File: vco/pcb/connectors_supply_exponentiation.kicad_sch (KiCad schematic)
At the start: 49 parts

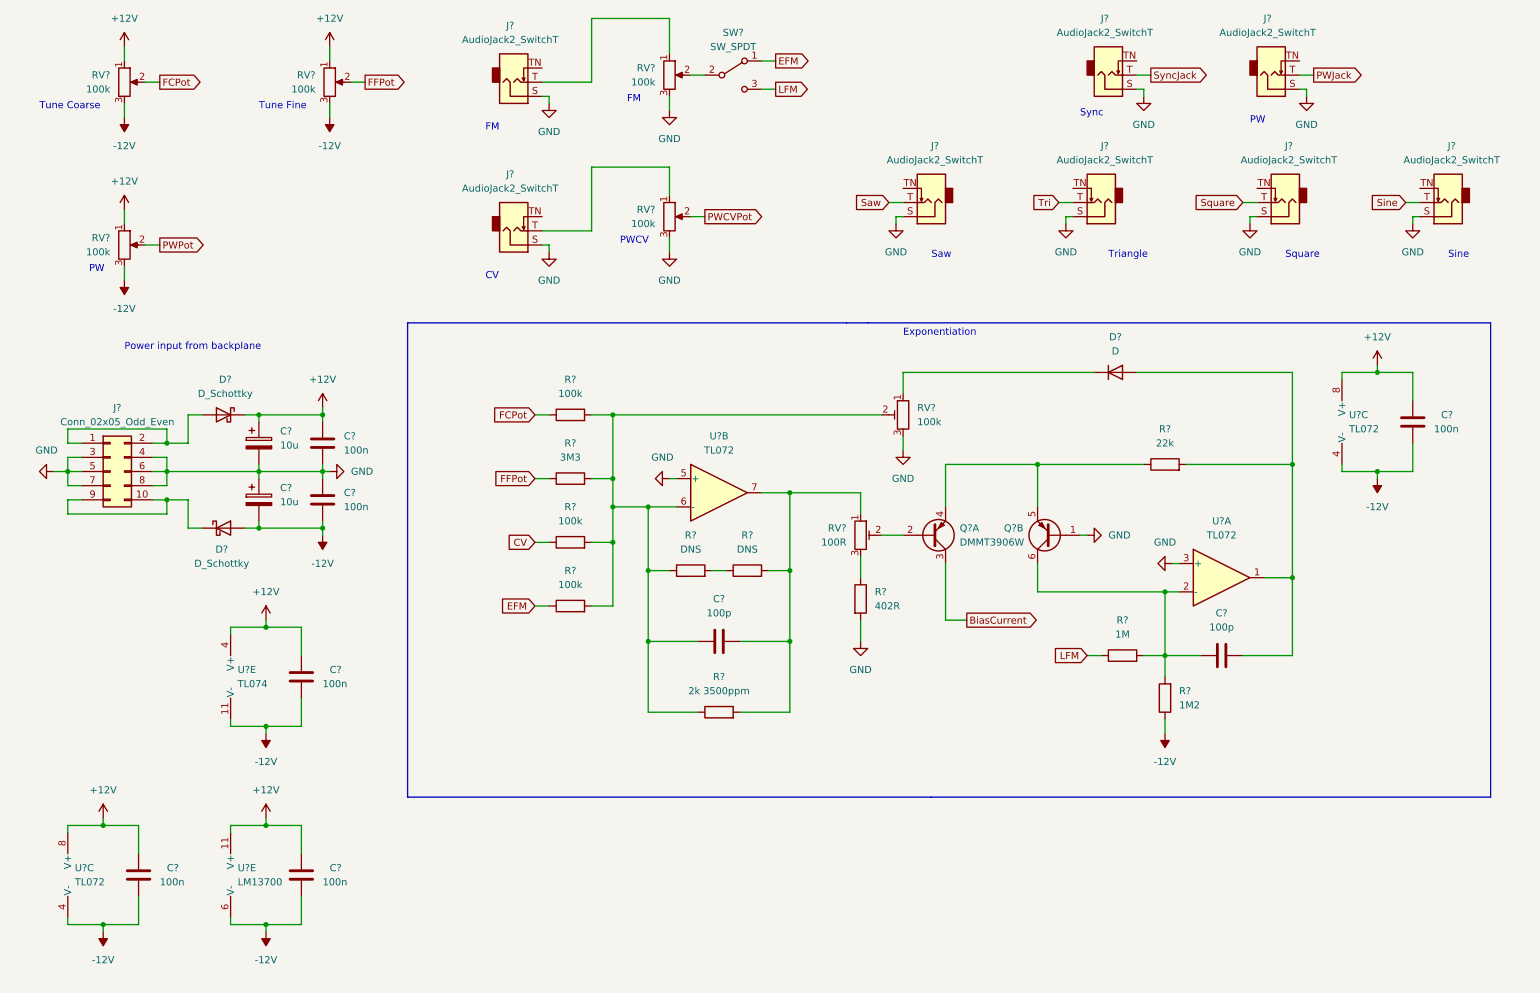
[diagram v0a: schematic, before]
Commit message: vco: Schematic update, footprints
- small changes to the schematic
- footprints assigned to all parts
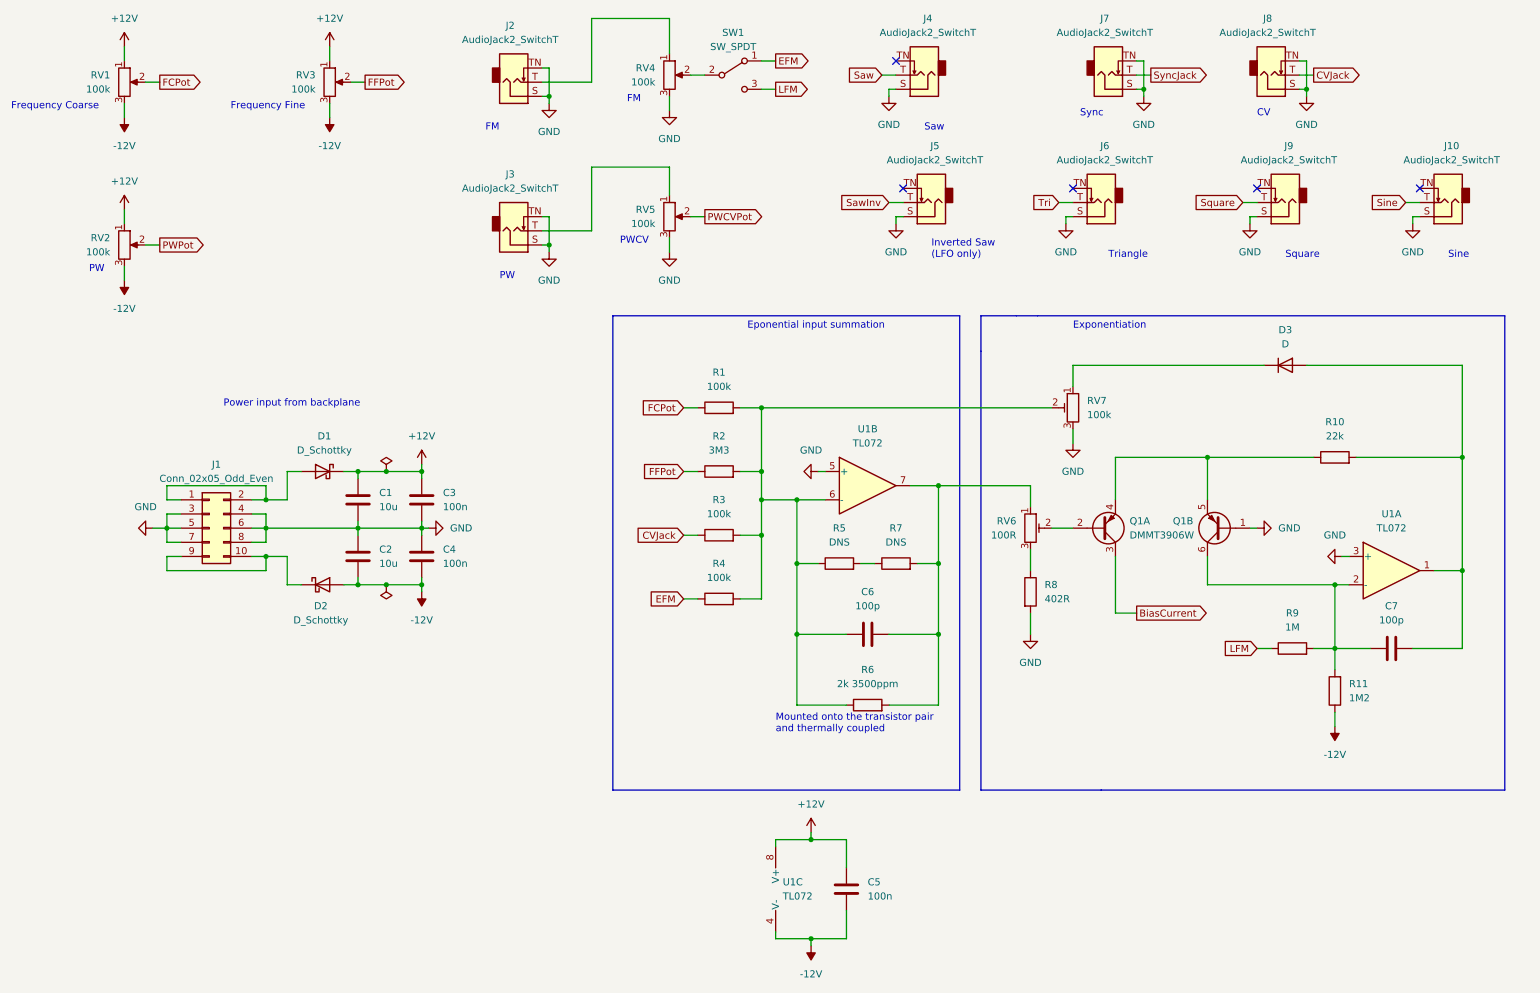
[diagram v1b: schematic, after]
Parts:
- removed C? (x3): 100n, symbol Device:C
- removed U?: TL074, symbol Amplifier_Operational:TL074
- removed U?: TL072, symbol Amplifier_Operational:TL072
- removed U?: LM13700, symbol Amplifier_Operational:LM13700
- added J4: AudioJack2_SwitchT, Connector_Audio:Jack_3.5mm_QingPu_WQP-PJ398SM_Vertical_CircularHoles, symbol Connector:AudioJack2_SwitchT
- C1, C2: renamed from C?; footprint (none) -> Capacitor_SMD:C_0603_1608Metric_Pad1.08x0.95mm_HandSolder; symbol Device:C_Polarized -> Device:C
- C3, C4, C5, C6, C7: renamed from C?; footprint (none) -> Capacitor_SMD:C_0603_1608Metric_Pad1.08x0.95mm_HandSolder
- D1, D2: renamed from D?; footprint (none) -> Diode_SMD:D_SMA_Handsoldering
- D3: renamed from D?; footprint (none) -> Diode_SMD:D_SOD-323_HandSoldering
- J1: renamed from J?; footprint (none) -> Connector_PinHeader_2.54mm:PinHeader_2x05_P2.54mm_Vertical
- J10, J2, J3, J5, J6, J7, J8, J9: renamed from J?; footprint (none) -> Connector_Audio:Jack_3.5mm_QingPu_WQP-PJ398SM_Vertical_CircularHoles
- R1, R10, R11, R2, R3, R4, R5, R7, R8, R9: renamed from R?; footprint (none) -> Resistor_SMD:R_0603_1608Metric_Pad0.98x0.95mm_HandSolder
- R6: renamed from R?; footprint (none) -> Resistor_THT:R_Axial_DIN0309_L9.0mm_D3.2mm_P15.24mm_Horizontal
- RV1, RV2, RV3, RV4, RV5: renamed from RV?; footprint (none) -> Potentiometer_THT:Potentiometer_Alpha_RD901F-40-00D_Single_Vertical
- RV6, RV7: renamed from RV?; footprint (none) -> Potentiometer_THT:Potentiometer_Bourns_3296W_Vertical
- SW1: renamed from SW?; footprint (none) -> Thonkiconn:Switch_Sub-Minitiature_Vertical
- U1: renamed from U?; footprint (none) -> Package_SO:SOIC-8_3.9x4.9mm_P1.27mm
- gave numbers to parts that had none: 1
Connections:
- net PWJack is gone; now on net CVJack: J8.T
- net GND: now also J2.TN, J3.TN, J7.TN, J8.TN, J4.S
- net Saw: now also J4.T; no longer J5.T
- net CV renamed CVJack
- new net SawInv: J5.T
- no-connect marks 0 -> 5
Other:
- note added: "Eponential input summation"
- note added: "Frequency Coarse"
- note added: "Frequency Fine"
- note added: "Inverted Saw (LFO only)"
- note added: "Mounted onto the transistor pair and thermally coupled"
- note removed: "Tune Coarse"
- note removed: "Tune Fine"
- title: (none) -> Input, Supply and Exponentiation
- moved on the sheet: C3, C4, C5, C6, C7, D1, D2, D3, J1, Q1A, Q1B, R1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

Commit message: vco: Add a note about the CV input range
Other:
- note added: "All inputs are -5V … +5V"
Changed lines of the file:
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@@
+    (effects (font (size 1.27 1.27)) (justify left bottom))
+  )
+  (text "All inputs are -5V … +5V" (at 255.27 40.64 0)
     (effects (font (size 1.27 1.27)) (justify left bottom))
   )

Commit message: vco: Layout WIP: component placement
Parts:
- D3: value D -> 1N4148
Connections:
- net EFM: now also SW1.3 (C); no longer SW1.1 (A)
- net LFM: now also SW1.1 (A); no longer SW1.3 (C)
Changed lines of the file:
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@@
     (in_bom yes) (on_board yes) (fields_autoplaced)
     (property "Reference" "D3" (id 0) (at 242.57 80.01 0))
-    (property "Value" "D" (id 1) (at 242.57 82.55 0))
+    (property "Value" "1N4148" (id 1) (at 242.57 82.55 0))
     (property "Footprint" "Diode_SMD:D_SOD-323_HandSoldering" (id 2) (at 242.57 86.36 0)
       (effects (font (size 1.27 1.27)) hide)
@@
     (pin "2")
   )
-  (symbol (lib_id "Switch:SW_SPDT") (at 143.51 34.29 0) (unit 1)
+  (symbol (lib_id "Switch:SW_SPDT") (at 143.51 34.29 0) (mirror x) (unit 1)
     (in_bom yes) (on_board yes) (fields_autoplaced)
     (property "Reference" "SW1" (id 0) (at 143.51 26.67 0))

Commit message: vco: Add Mouser order codes
Add Mouser order codes to some parts.  THis solution isn't really nice, though.
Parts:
- D1, D2: value D_Schottky -> B130-13F; Mouser (none) -> 621-B130-F
- D3: Mouser (none) -> 512-1N4148WS
- J1: Mouser (none) -> 200-TSW10507GD
- Q1: Mouser (none) -> 621-DMMT3906W-F
- U1: Mouser (none) -> 595-TL072CDR
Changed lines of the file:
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@@
+      (effects (font (size 1.27 1.27)) hide)
+    )
+    (property "Mouser" "595-TL072CDR " (id 4) (at 261.62 123.19 0)
       (effects (font (size 1.27 1.27)) hide)
     )
@@
     (in_bom yes) (on_board yes) (fields_autoplaced)
     (property "Reference" "D1" (id 0) (at 70.1675 99.06 0))
-    (property "Value" "D_Schottky" (id 1) (at 70.1675 101.6 0))
+    (property "Value" "B130-13F" (id 1) (at 70.1675 101.6 0))
     (property "Footprint" "Diode_SMD:D_SMA_Handsoldering" (id 2) (at 69.85 105.41 0)
       (effects (font (size 1.27 1.27)) hide)
     )
-    (property "Datasheet" "~" (id 3) (at 69.85 105.41 0)
+    (property "Datasheet" "https://www.diodes.com/assets/Datasheets/ds13002.pdf" (id 3) (at 69.85 105.41 0)
+      (effects (font (size 1.27 1.27)) hide)
+    )
+    (property "Mouser" " 621-B130-F " (id 4) (at 69.85 105.41 0)
       (effects (font (size 1.27 1.27)) hide)
     )
@@
     )
     (property "Datasheet" "http://www.ti.com/lit/ds/symlink/tl071.pdf" (id 3) (at 153.67 180.34 0)
+      (effects (font (size 1.27 1.27)) hide)
+    )
+    (property "Mouser" "595-TL072CDR " (id 4) (at 153.67 180.34 0)
       (effects (font (size 1.27 1.27)) hide)
     )
@@
       (effects (font (size 1.27 1.27)) hide)
     )
+    (property "Mouser" " 621-DMMT3906W-F " (id 4) (at 209.55 115.57 0)
+      (effects (font (size 1.27 1.27)) hide)
+    )
     (pin "2")
     (pin "3")
@@
     (in_bom yes) (on_board yes) (fields_autoplaced)
     (property "Reference" "D2" (id 0) (at 69.5325 129.54 0))
-    (property "Value" "D_Schottky" (id 1) (at 69.5325 132.08 0))
+    (property "Value" "B130-13F" (id 1) (at 69.5325 132.08 0))
     (property "Footprint" "Diode_SMD:D_SMA_Handsoldering" (id 2) (at 69.85 125.73 0)
       (effects (font (size 1.27 1.27)) hide)
     )
-    (property "Datasheet" "~" (id 3) (at 69.85 125.73 0)
+    (property "Datasheet" "https://www.diodes.com/assets/Datasheets/ds13002.pdf" (id 3) (at 69.85 125.73 0)
+      (effects (font (size 1.27 1.27)) hide)
+    )
+    (property "Mouser" " 621-B130-F " (id 4) (at 69.85 125.73 0)
       (effects (font (size 1.27 1.27)) hide)
     )
@@
     )
     (property "Datasheet" "~" (id 3) (at 49.53 115.57 0)
+      (effects (font (size 1.27 1.27)) hide)
+    )
+    (property "Mouser" " 200-TSW10507GD " (id 4) (at 49.53 115.57 0)
       (effects (font (size 1.27 1.27)) hide)
     )
@@
       (effects (font (size 1.27 1.27)) hide)
     )
+    (property "Mouser" "595-TL072CDR " (id 4) (at 167.64 107.95 0)
+      (effects (font (size 1.27 1.27)) hide)
+    )
     (pin "1")
     (pin "2")
@@
       (effects (font (size 1.27 1.27)) hide)
     )
+    (property "Mouser" " 512-1N4148WS " (id 4) (at 242.57 86.36 0)
+      (effects (font (size 1.27 1.27)) hide)
+    )
     (pin "1")
     (pin "2")
@@
       (effects (font (size 1.27 1.27)) hide)
     )
+    (property "Mouser" " 621-DMMT3906W-F " (id 4) (at 231.14 115.57 0)
+      (effects (font (size 1.27 1.27)) hide)
+    )

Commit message: vco: Add more info to silk
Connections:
- net at J1.1 (Pin_1), J1.2 (Pin_2): now also D2.1 (K); no longer D1.2 (A)
- net at J1.10 (Pin_10), J1.9 (Pin_9): now also D1.2 (A); no longer D2.1 (K)
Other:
- note added: "1V/oct adj"
- note added: "CV (V/oct)"
- note added: "HF adj"
- note removed: "CV"
- moved on the sheet: J1
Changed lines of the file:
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@@
+    (effects (font (size 1.27 1.27)) (justify left bottom))
+  )
+  (text "HF adj" (at 207.01 99.06 0)
     (effects (font (size 1.27 1.27)) (justify left bottom))
   )
   (text "FM" (at 99.06 44.45 0)
+    (effects (font (size 1.27 1.27)) (justify left bottom))
+  )
+  (text "1V/oct\nadj" (at 189.23 123.19 0)
     (effects (font (size 1.27 1.27)) (justify left bottom))
   )
@@
     (effects (font (size 1.27 1.27)) (justify left bottom))
   )
-  (text "CV" (at 237.49 41.91 0)
+  (text "CV (V/oct)" (at 232.41 41.91 0)
     (effects (font (size 1.27 1.27)) (justify left bottom))
   )
@@
     (pin "1")
   )
-  (symbol (lib_id "Connector_Generic:Conn_02x05_Odd_Even") (at 49.53 115.57 0) (unit 1)
+  (symbol (lib_id "Connector_Generic:Conn_02x05_Odd_Even") (at 52.07 115.57 180) (unit 1)
     (in_bom yes) (on_board yes) (fields_autoplaced)
     (property "Reference" "J1" (id 0) (at 50.8 104.14 0))
     (property "Value" "Conn_02x05_Odd_Even" (id 1) (at 50.8 106.68 0))
-    (property "Footprint" "Connector_PinHeader_2.54mm:PinHeader_2x05_P2.54mm_Vertical" (id 2) (at 49.53 115.57 0)
-      (effects (font (size 1.27 1.27)) hide)
-    )
-    (property "Datasheet" "~" (id 3) (at 49.53 115.57 0)
-      (effects (font (size 1.27 1.27)) hide)
-    )
-    (property "Mouser" " 200-TSW10507GD " (id 4) (at 49.53 115.57 0)
-      (effects (font (size 1.27 1.27)) hide)
-    )
+    (property "Footprint" "Connector_PinHeader_2.54mm:PinHeader_2x05_P2.54mm_Vertical" (id 2) (at 52.07 115.57 0)
+      (effects (font (size 1.27 1.27)) hide)
+    )
+    (property "Datasheet" "~" (id 3) (at 52.07 115.57 0)
+      (effects (font (size 1.27 1.27)) hide)
+    )
+    (property "Mouser" " 200-TSW10507GD " (id 4) (at 52.07 115.57 0)
+      (effects (font (size 1.27 1.27)) hide)
+    )

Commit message: vco: Update headers in pcb
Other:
- company: (none) -> L. Rittel
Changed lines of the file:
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@@
   (title_block
     (title "Input, Supply and Exponentiation")
-    (date "2022-12-30")
-    (rev "Rev. 1")
+    (date "2022-12-31")
+    (rev "Rev. 1 2022")
+    (company "L. Rittel")
   )
   (junction (at 76.2 115.57) (diameter 0) (color 0 0 0 0)

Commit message: vco: Small update
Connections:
- net GND: no longer J2.TN, J3.TN, J7.TN, J8.TN
- no-connect marks 5 -> 9
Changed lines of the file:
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@@
   (junction (at 154.94 134.62) (diameter 0) (color 0 0 0 0)
   )
-  (junction (at 110.49 64.77) (diameter 0) (color 0 0 0 0)
-  )
   (junction (at 180.34 134.62) (diameter 0) (color 0 0 0 0)
   )
-  (junction (at 110.49 38.1) (diameter 0) (color 0 0 0 0)
-  )
   (junction (at 59.69 110.49) (diameter 0) (color 0 0 0 0)
   )
@@
   (junction (at 87.63 125.73) (diameter 0) (color 0 0 0 0)
   )
-  (junction (at 246.38 36.83) (diameter 0) (color 0 0 0 0)
-  )
   (junction (at 157.48 171.45) (diameter 0) (color 0 0 0 0)
   )
@@
   (junction (at 59.69 115.57) (diameter 0) (color 0 0 0 0)
   )
-  (junction (at 217.17 36.83) (diameter 0) (color 0 0 0 0)
-  )
   (junction (at 274.32 123.19) (diameter 0) (color 0 0 0 0)
   )
@@
   )
   (no_connect (at 266.7 54.61))
+  (no_connect (at 109.22 33.02))
+  (no_connect (at 245.11 31.75))
+  (no_connect (at 215.9 31.75))
+  (no_connect (at 109.22 59.69))
   (no_connect (at 172.72 31.75))
   (no_connect (at 204.47 54.61))
@@
     (stroke (width 0) (type default) (color 0 0 0 0))
   )
-  (wire (pts (xy 109.22 59.69) (xy 110.49 59.69))
-    (stroke (width 0) (type default) (color 0 0 0 0))
-  )
   (wire (pts (xy 44.45 110.49) (xy 41.91 110.49))
     (stroke (width 0) (type default) (color 0 0 0 0))
@@
     (stroke (width 0) (type default) (color 0 0 0 0))
   )
-  (wire (pts (xy 217.17 31.75) (xy 215.9 31.75))
-    (stroke (width 0) (type default) (color 0 0 0 0))
-  )
   (wire (pts (xy 157.48 189.23) (xy 151.13 189.23))
     (stroke (width 0) (type default) (color 0 0 0 0))
@@
     (stroke (width 0) (type default) (color 0 0 0 0))
   )
-  (wire (pts (xy 110.49 59.69) (xy 110.49 64.77))
-    (stroke (width 0) (type default) (color 0 0 0 0))
-  )
   (wire (pts (xy 38.1 35.56) (xy 40.64 35.56))
     (stroke (width 0) (type default) (color 0 0 0 0))
@@
     (stroke (width 0) (type default) (color 0 0 0 0))
   )
-  (wire (pts (xy 246.38 31.75) (xy 246.38 36.83))
-    (stroke (width 0) (type default) (color 0 0 0 0))
-  )
   (wire (pts (xy 204.47 90.17) (xy 204.47 86.36))
     (stroke (width 0) (type default) (color 0 0 0 0))
@@
     (stroke (width 0) (type default) (color 0 0 0 0))
   )
-  (wire (pts (xy 110.49 38.1) (xy 110.49 33.02))
-    (stroke (width 0) (type default) (color 0 0 0 0))
-  )
   (wire (pts (xy 171.45 147.32) (xy 180.34 147.32))
     (stroke (width 0) (type default) (color 0 0 0 0))
@@
     (stroke (width 0) (type default) (color 0 0 0 0))
   )
-  (wire (pts (xy 245.11 31.75) (xy 246.38 31.75))
-    (stroke (width 0) (type default) (color 0 0 0 0))
-  )
   (wire (pts (xy 87.63 114.3) (xy 87.63 115.57))
     (stroke (width 0) (type default) (color 0 0 0 0))
@@
     (stroke (width 0) (type default) (color 0 0 0 0))
   )
-  (wire (pts (xy 217.17 36.83) (xy 217.17 31.75))
-    (stroke (width 0) (type default) (color 0 0 0 0))
-  )
   (wire (pts (xy 59.69 115.57) (xy 59.69 113.03))
     (stroke (width 0) (type default) (color 0 0 0 0))
@@
     (stroke (width 0) (type default) (color 0 0 0 0))
   )
-  (wire (pts (xy 110.49 33.02) (xy 109.22 33.02))
-    (stroke (width 0) (type default) (color 0 0 0 0))
-  )
